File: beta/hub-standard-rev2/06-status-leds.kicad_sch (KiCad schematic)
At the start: 10 parts, among them U6 SN74AHCT1G08

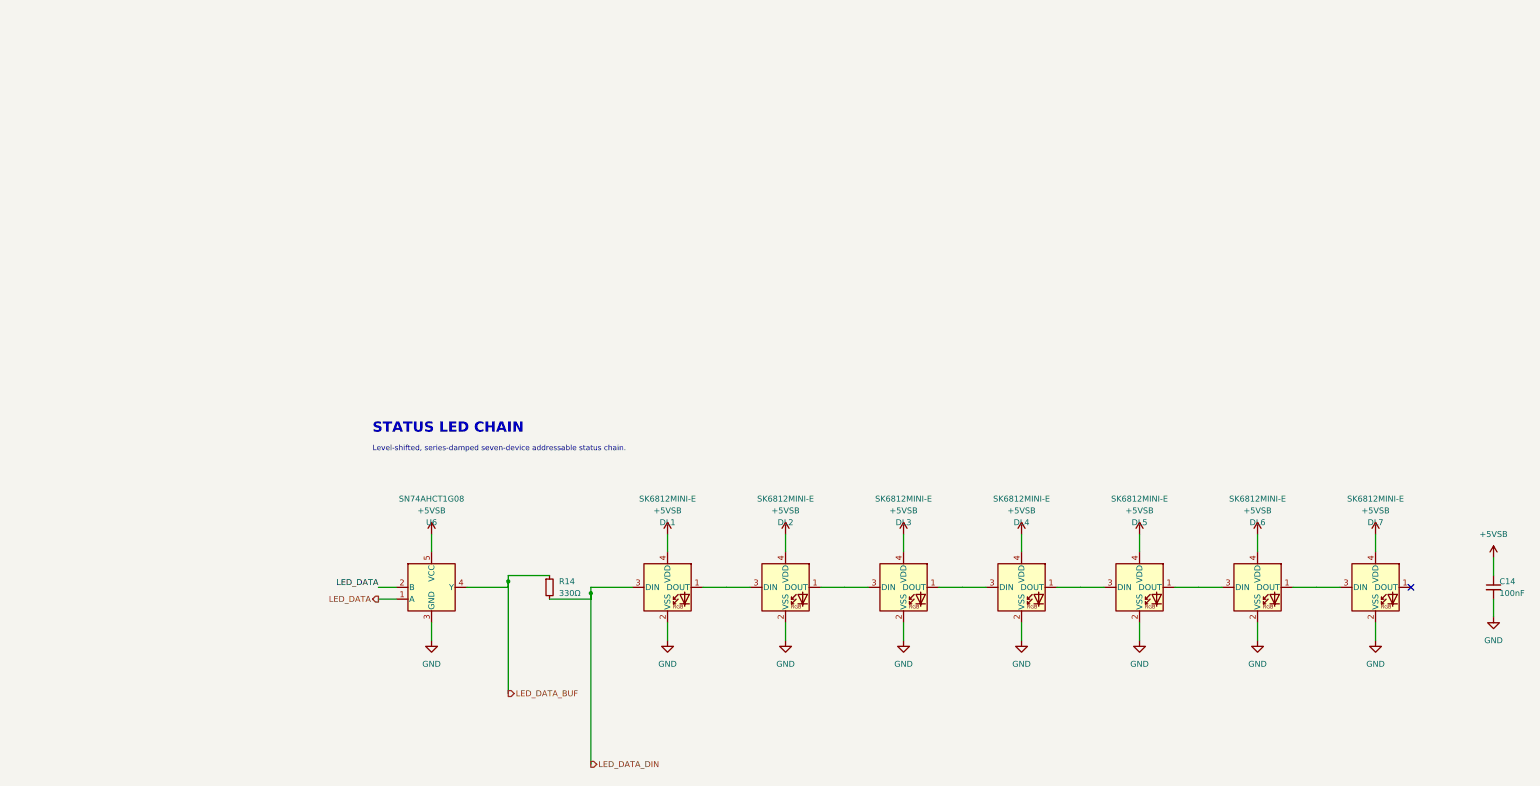
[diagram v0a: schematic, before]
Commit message: Enforce readable BETA schematic layouts
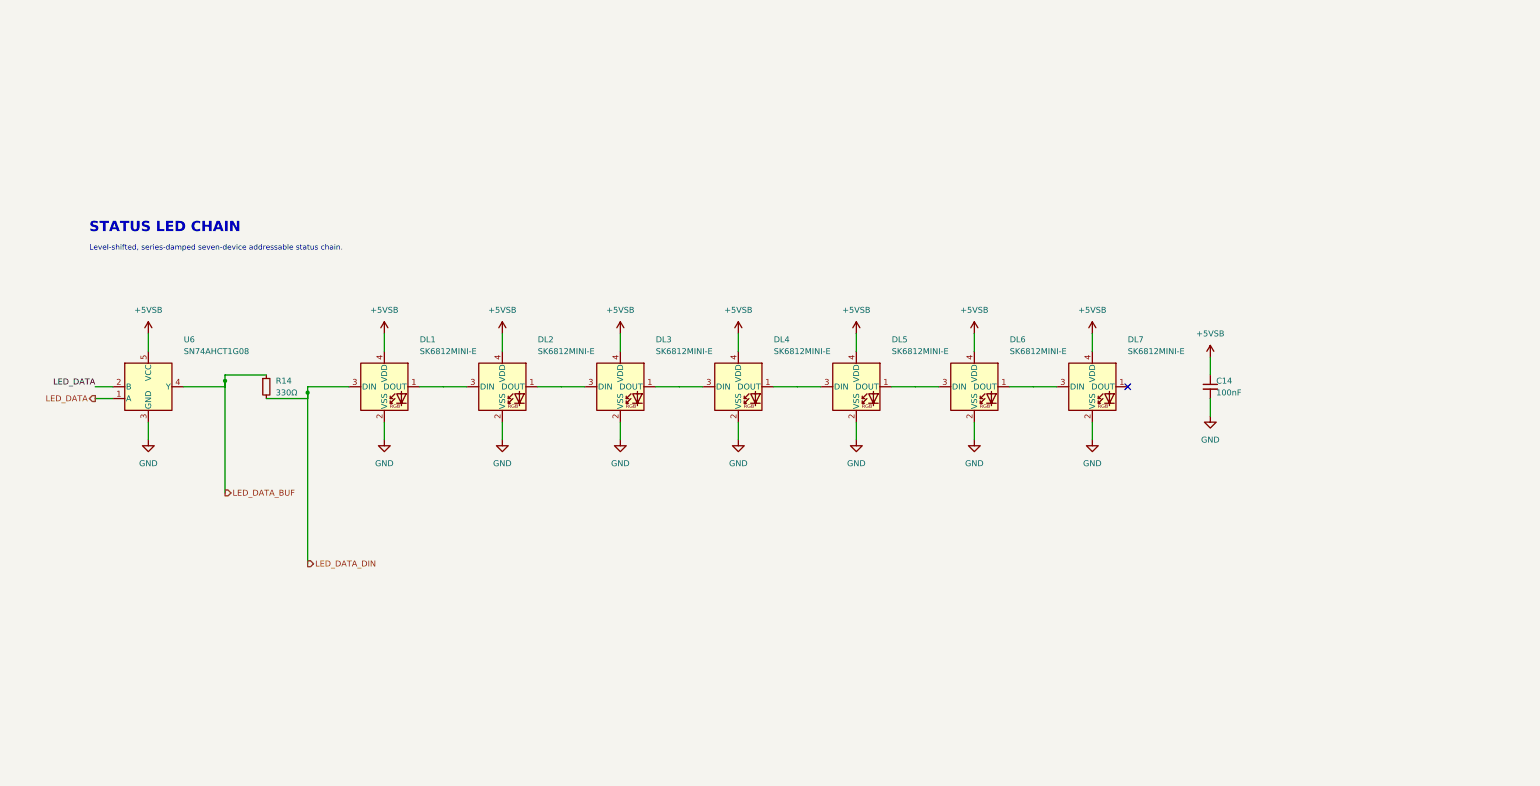
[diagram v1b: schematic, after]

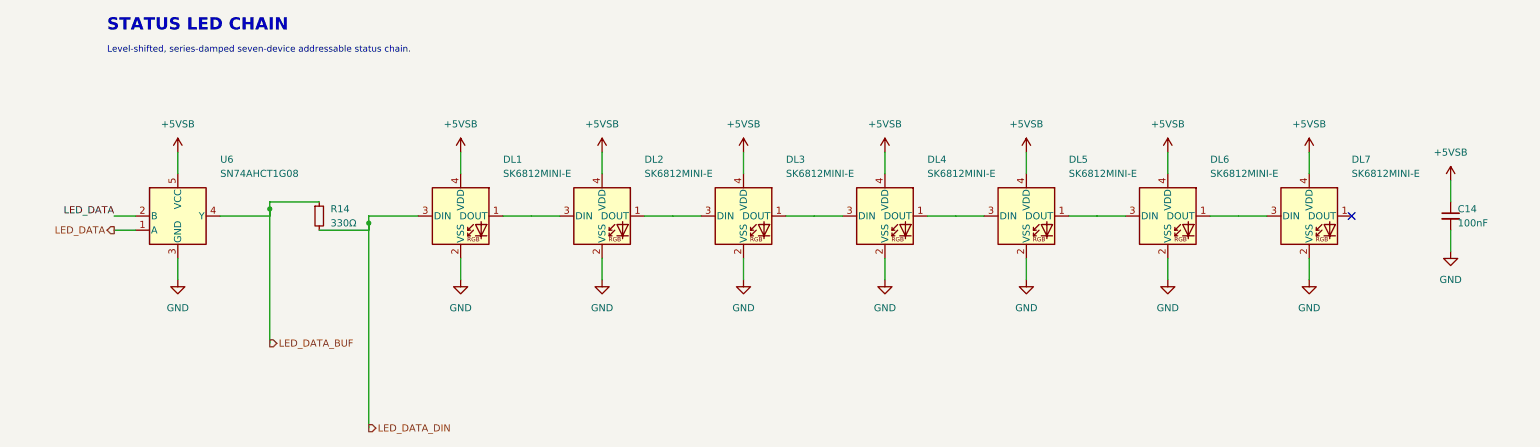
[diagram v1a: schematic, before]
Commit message: Rework BETA power rails and schematic composition
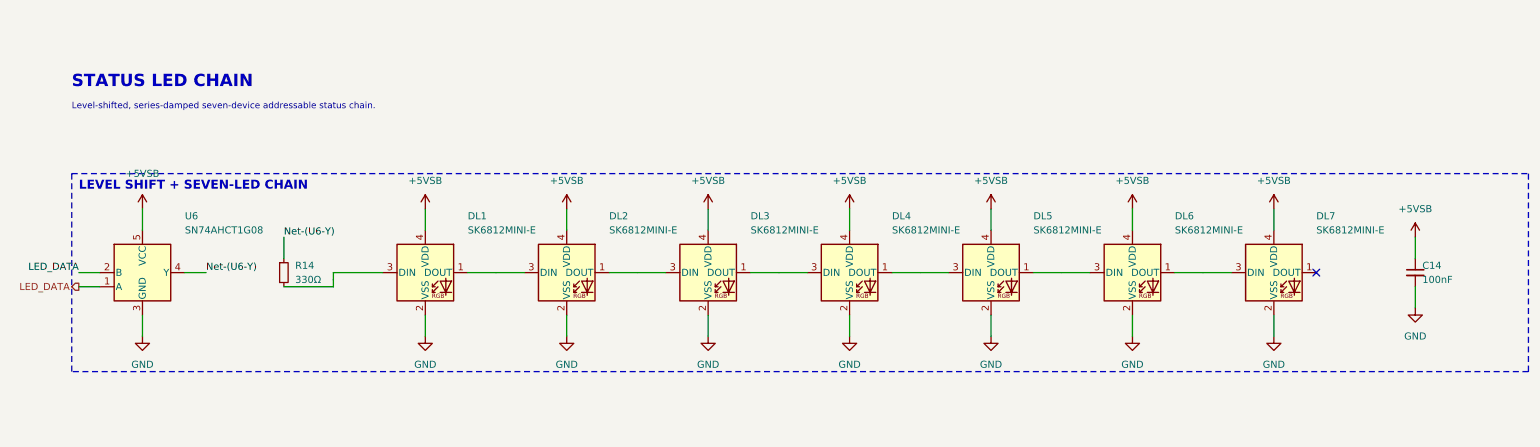
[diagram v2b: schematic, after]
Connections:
- net LED_DATA_BUF renamed Net-(U6-Y)
- net LED_DATA_DIN: no longer names the net of DL1.3 (DIN), R14.2
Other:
- note added: "LEVEL SHIFT + SEVEN-LED CHAIN"

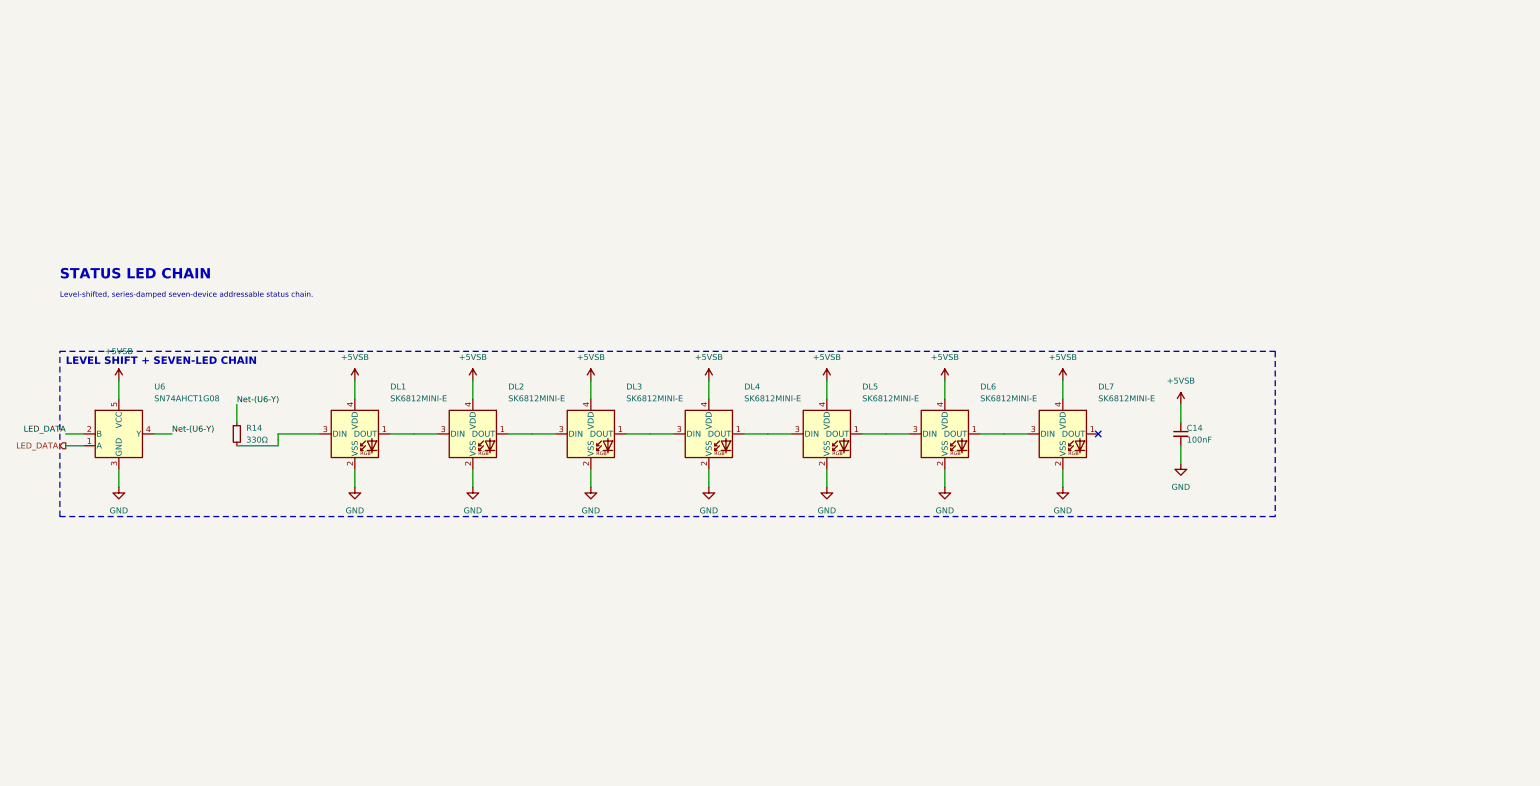
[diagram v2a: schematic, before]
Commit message: Finalize compact Hub and ATX power-layout audit
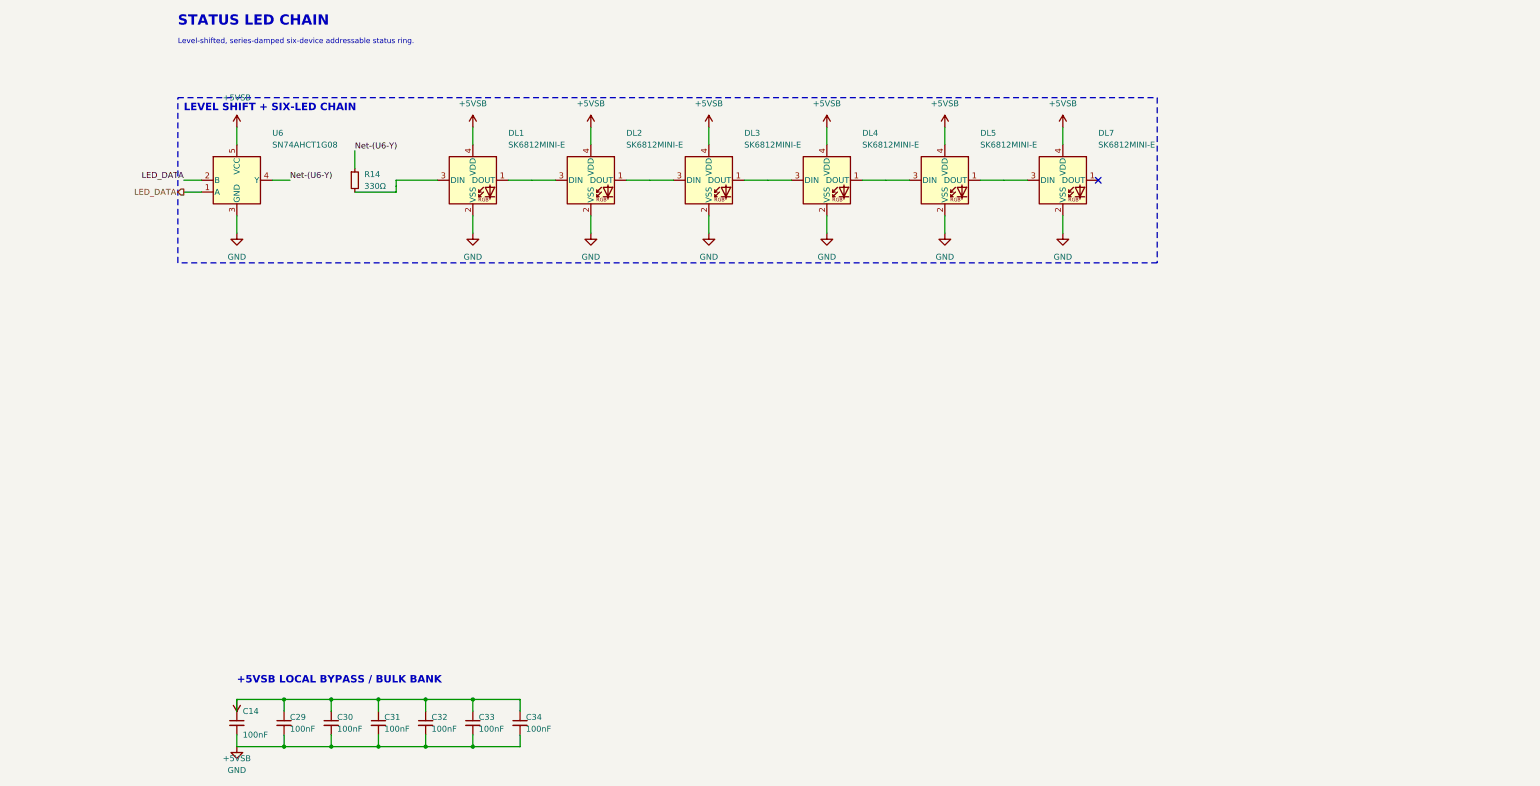
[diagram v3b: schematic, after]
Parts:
- removed DL6: SK6812MINI-E, cec-LED_SMD:LED_SK6812MINI_PLCC4_3.5x3.5mm_P1.75mm, symbol cec-vendor:SK6812MINI
- added C29, C30, C31, C32, C33, C34: 100nF, cec-Capacitor_SMD:C_0402_1005Metric, symbol cec-vendor:C_Small
- C14: Note (none) -> SN74AHCT1G08 U6 local 100nF bypass; place directly at VCC/G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
- DL1, DL2, DL3, DL4, DL5, DL7: footprint cec-LED_SMD:LED_SK6812MINI_PLCC4_3.5x3.5mm_P1.75mm -> cec-LED_SMD:LED_SK6812MINI-E_3.2x2.8mm_P1.5mm_ReverseMount; Manufacturer Opsco -> OPSCO Optoelectronics
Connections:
- net +5VSB: now also C29.1, C30.1, C31.1, C32.1, C33.1, C34.1
- net GND: now also C29.2, C30.2, C31.2, C32.2, C33.2, C34.2
- net at DL5.1 (DOUT): now also DL7.3 (DIN)
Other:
- note added: "+5VSB LOCAL BYPASS / BULK BANK"
- note added: "LEVEL SHIFT + SIX-LED CHAIN"
- note added: "Level-shifted, series-damped six-device addressable status ring."
- note removed: "LEVEL SHIFT + SEVEN-LED CHAIN"
- note removed: "Level-shifted, series-damped seven-device addressable status chain."
